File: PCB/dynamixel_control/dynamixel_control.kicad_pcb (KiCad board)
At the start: 4 copper layers, 36 x 56 mm, 57 parts, among them J1 12V, J11 Dynamixel TTL, J12 Dynamixel TTL, J2 RS232, J3 5V, J4 3.3V, J5 I2C, J6 Debug Uart, J8 Dynamixel TTL, Q1 SSM3J372R, Q2 IPD068P03L3GATMA1, Q3 T2N7002AK, SW1 LIMIT_SWITCH, U1 R-78E5.0-0.5, U2 SN74AHC1G14, U3 LM810M3-4.63, U4 Teensy_4.0, U5 MAX3221E, U6 ICM-40627, U7 SN74LV1T34, U8 SN74LVC2G241

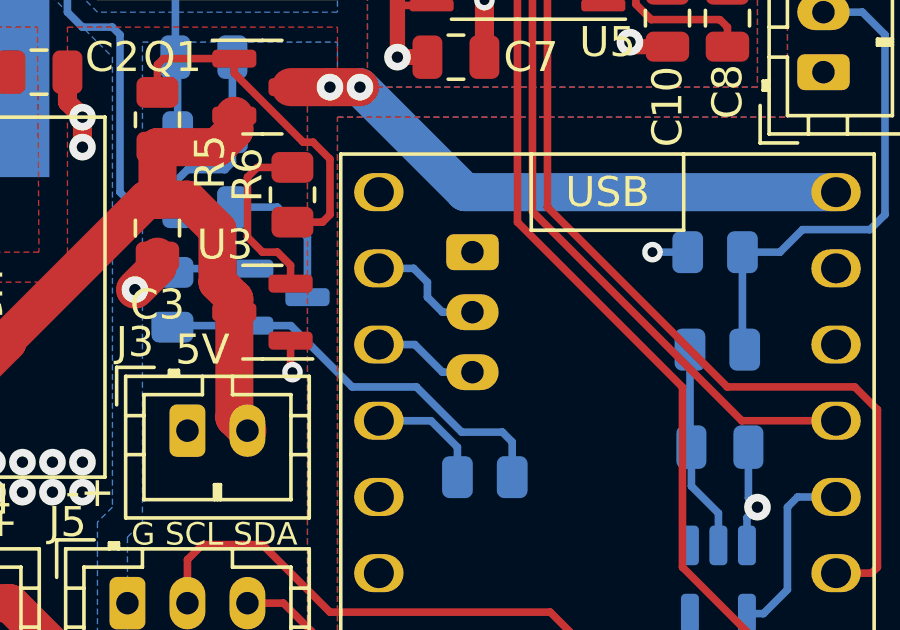
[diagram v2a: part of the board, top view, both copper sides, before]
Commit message: Change MAX3221E by SN65C3221E.
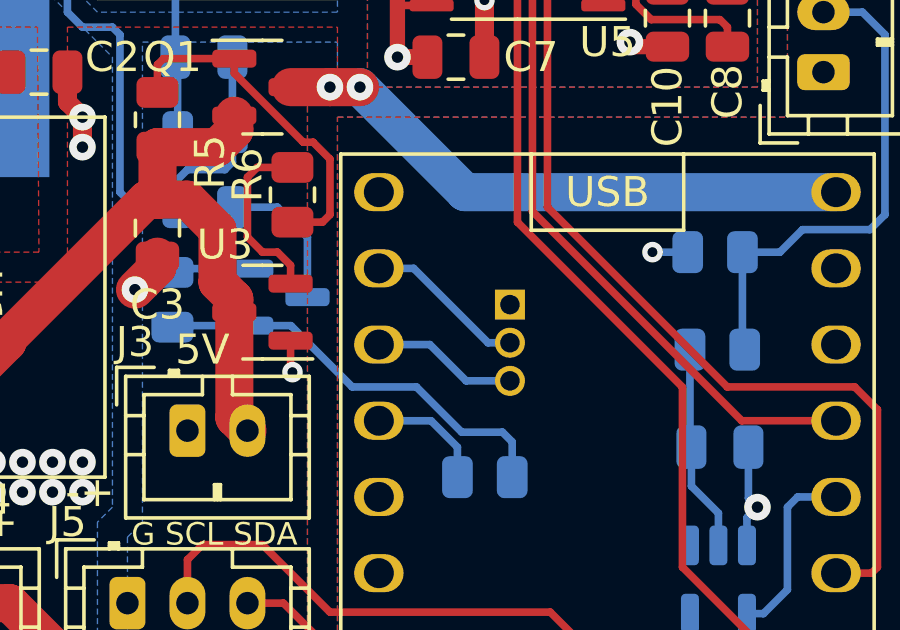
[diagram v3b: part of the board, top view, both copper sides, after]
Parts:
- J6: footprint Connector_JST:JST_PH_B3B-PH-K_1x03_P2.00mm_Vertical -> Connector_PinHeader_1.27mm:PinHeader_1x03_P1.27mm_Vertical
- U5: value MAX3221E -> SN65C3221E
- moved J6 2.15 mm to (42.2, 44.2), turned to 180 degrees
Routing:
- net /DEBUG_UART_RX: track 4.02 -> 5.40 mm
- net /DEBUG_UART_TX: track 3.50 -> 4.87 mm
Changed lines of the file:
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@@
       (effects (font (size 1 1) (thickness 0.15)))
     )
-    (fp_text value "MAX3221E" (at 0 3.45) (layer "F.Fab")
+    (fp_text value "SN65C3221E" (at 0 3.45) (layer "F.Fab")
       (effects (font (size 1 1) (thickness 0.15)))
     )
@@
     )
   )
-  (footprint "Connector_JST:JST_PH_B3B-PH-K_1x03_P2.00mm_Vertical" (layer "B.Cu")
-    (at 41 42.5 -90)
-    (descr "JST PH series connector, B3B-PH-K (http://www.jst-mfg.com/product/pdf/eng/ePH.pdf), generated with kicad-footprint-generator")
-    (tags "connector JST PH side entry")
-    (property "Sheetfile" "dynamixel_control.kicad_sch")
-    (property "Sheetname" "")
-    (attr through_hole)
-    (fp_text reference "J6" (at -1.5 -4 180) (layer "B.SilkS")
-      (effects (font (size 1 1) (thickness 0.15)) (justify mirror))
-    )
-    (fp_text value "Debug Uart" (at 2 -4 90) (layer "B.Fab")
-      (effects (font (size 1 1) (thickness 0.15)) (justify mirror))
-    )
-    (fp_text user "${REFERENCE}" (at 2 -1.5 90) (layer "B.Fab")
-      (effects (font (size 1 1) (thickness 0.15)) (justify mirror))
-    )
-    (fp_line (start 5.45 -2.3) (end 5.45 1.2) (layer "B.SilkS") (width 0.12))
-    (fp_line (start -2.36 2.11) (end -2.36 0.86) (layer "B.SilkS") (width 0.12))
-    (fp_line (start -2.06 -0.8) (end -1.45 -0.8) (layer "B.SilkS") (width 0.12))
-    (fp_line (start 0.9 -1.8) (end 1.1 -1.8) (layer "B.SilkS") (width 0.12))
-    (fp_line (start -1.11 2.11) (end -2.36 2.11) (layer "B.SilkS") (width 0.12))
-    (fp_line (start 0.5 1.81) (end 0.5 1.2) (layer "B.SilkS") (width 0.12))
-    (fp_line (start -2.06 -2.91) (end 6.06 -2.91) (layer "B.SilkS") (width 0.12))
-    (fp_line (start 1.1 -1.8) (end 1.1 -2.3) (layer "B.SilkS") (width 0.12))
-    (fp_line (start -0.3 1.91) (end -0.6 1.91) (layer "B.SilkS") (width 0.12))
-    (fp_line (start 5.45 1.2) (end 3.5 1.2) (layer "B.SilkS") (width 0.12))
-    (fp_line (start 3.5 1.2) (end 3.5 1.81) (layer "B.SilkS") (width 0.12))
-    (fp_line (start 0.9 -2.3) (end 0.9 -1.8) (layer "B.SilkS") (width 0.12))
-    (fp_line (start -1.45 -2.3) (end 5.45 -2.3) (layer "B.SilkS") (width 0.12))
-    (fp_line (start 6.06 1.81) (end -2.06 1.81) (layer "B.SilkS") (width 0.12))
-    (fp_line (start 6.06 -2.91) (end 6.06 1.81) (layer "B.SilkS") (width 0.12))
-    (fp_line (start 2.9 -2.3) (end 2.9 -1.8) (layer "B.SilkS") (width 0.12))
-    (fp_line (start 2.9 -1.8) (end 3.1 -1.8) (layer "B.SilkS") (width 0.12))
-    (fp_line (start 3 -2.3) (end 3 -1.8) (layer "B.SilkS") (width 0.12))
-    (fp_line (start -1.45 1.2) (end -1.45 -2.3) (layer "B.SilkS") (width 0.12))
-    (fp_line (start 0.5 1.2) (end -1.45 1.2) (layer "B.SilkS") (width 0.12))
-    (fp_line (start -0.6 2.01) (end -0.6 1.81) (layer "B.SilkS") (width 0.12))
-    (fp_line (start -0.3 2.01) (end -0.6 2.01) (layer "B.SilkS") (width 0.12))
-    (fp_line (start 6.06 -0.8) (end 5.45 -0.8) (layer "B.SilkS") (width 0.12))
-    (fp_line (start 6.06 0.5) (end 5.45 0.5) (layer "B.SilkS") (width 0.12))
-    (fp_line (start -2.06 0.5) (end -1.45 0.5) (layer "B.SilkS") (width 0.12))
-    (fp_line (start 1 -2.3) (end 1 -1.8) (layer "B.SilkS") (width 0.12))
-    (fp_line (start 3.1 -1.8) (end 3.1 -2.3) (layer "B.SilkS") (width 0.12))
-    (fp_line (start -2.06 1.81) (end -2.06 -2.91) (layer "B.SilkS") (width 0.12))
-    (fp_line (start -0.3 1.81) (end -0.3 2.01) (layer "B.SilkS") (width 0.12))
-    (fp_line (start -2.45 -3.3) (end 6.45 -3.3) (layer "B.CrtYd") (width 0.05))
-    (fp_line (start 6.45 2.2) (end -2.45 2.2) (layer "B.CrtYd") (width 0.05))
-    (fp_line (start -2.45 2.2) (end -2.45 -3.3) (layer "B.CrtYd") (width 0.05))
-    (fp_line (start 6.45 -3.3) (end 6.45 2.2) (layer "B.CrtYd") (width 0.05))
-    (fp_line (start -1.95 1.7) (end -1.95 -2.8) (layer "B.Fab") (width 0.1))
-    (fp_line (start -1.11 2.11) (end -2.36 2.11) (layer "B.Fab") (width 0.1))
-    (fp_line (start 5.95 1.7) (end -1.95 1.7) (layer "B.Fab") (width 0.1))
-    (fp_line (start -2.36 2.11) (end -2.36 0.86) (layer "B.Fab") (width 0.1))
-    (fp_line (start 5.95 -2.8) (end 5.95 1.7) (layer "B.Fab") (width 0.1))
-    (fp_line (start -1.95 -2.8) (end 5.95 -2.8) (layer "B.Fab") (width 0.1))
-    (pad "1" thru_hole roundrect (at 0 0 270) (size 1.2 1.75) (drill 0.75) (layers *.Cu *.Mask) (roundrect_rratio 0.208333)
-      (net 2 "GND") (pinfunction "Pin_1") (pintype "passive"))
-    (pad "2" thru_hole oval (at 2 0 270) (size 1.2 1.75) (drill 0.75) (layers *.Cu *.Mask)
-      (net 50 "/DEBUG_UART_RX") (pinfunction "Pin_2") (pintype "passive"))
-    (pad "3" thru_hole oval (at 4 0 270) (size 1.2 1.75) (drill 0.75) (layers *.Cu *.Mask)
-      (net 51 "/DEBUG_UART_TX") (pinfunction "Pin_3") (pintype "passive"))
-    (model "${KICAD6_3DMODEL_DIR}/Connector_JST.3dshapes/JST_PH_B3B-PH-K_1x03_P2.00mm_Vertical.wrl"
-      (offset (xyz 0 0 0))
-      (scale (xyz 1 1 1))
-      (rotate (xyz 0 0 0))
-    )
-  )
   (footprint "Resistor_SMD:R_0805_2012Metric" (layer "B.Cu")
     (at 49.0875 42.5)
@@
       (net 6 "Net-(C5-Pad1)") (pintype "passive"))
     (model "${KICAD6_3DMODEL_DIR}/Resistor_SMD.3dshapes/R_0805_2012Metric.wrl"
+      (offset (xyz 0 0 0))
+      (scale (xyz 1 1 1))
+      (rotate (xyz 0 0 0))
+    )
+  )
+  (footprint "Connector_PinHeader_1.27mm:PinHeader_1x03_P1.27mm_Vertical" (layer "B.Cu")
+    (at 42.25 44.25 180)
+    (descr "Through hole straight pin header, 1x03, 1.27mm pitch, single row")
+    (tags "Through hole pin header THT 1x03 1.27mm single row")
+    (property "Sheetfile" "dynamixel_control.kicad_sch")
+    (property "Sheetname" "")
+    (attr through_hole)
+    (fp_text reference "J6" (at 0 1.695) (layer "B.SilkS")
+      (effects (font (size 1 1) (thickness 0.15)) (justify mirror))
+    )
+    (fp_text value "Debug Uart" (at 0 -4.235) (layer "B.Fab")
+      (effects (font (size 1 1) (thickness 0.15)) (justify mirror))
+    )
+    (fp_text user "${REFERENCE}" (at 0 -1.27 90) (layer "B.Fab")
+      (effects (font (size 1 1) (thickness 0.15)) (justify mirror))
+    )
+    (fp_line (start -1.11 -0.76) (end -1.11 -3.235) (layer "B.SilkS") (width 0.12))
+    (fp_line (start 0.563471 -0.76) (end 1.11 -0.76) (layer "B.SilkS") (width 0.12))
+    (fp_line (start 1.11 -0.76) (end 1.11 -3.235) (layer "B.SilkS") (width 0.12))
+    (fp_line (start -1.11 0) (end -1.11 0.76) (layer "B.SilkS") (width 0.12))
+    (fp_line (start -1.11 0.76) (end 0 0.76) (layer "B.SilkS") (width 0.12))
+    (fp_line (start -1.11 -0.76) (end -0.563471 -0.76) (layer "B.SilkS") (width 0.12))
+    (fp_line (start 0.30753 -3.235) (end 1.11 -3.235) (layer "B.SilkS") (width 0.12))
+    (fp_line (start -1.11 -3.235) (end -0.30753 -3.235) (layer "B.SilkS") (width 0.12))
+    (fp_line (start -1.55 -3.7) (end 1.55 -3.7) (layer "B.CrtYd") (width 0.05))
+    (fp_line (start -1.55 1.15) (end -1.55 -3.7) (layer "B.CrtYd") (width 0.05))
+    (fp_line (start 1.55 1.15) (end -1.55 1.15) (layer "B.CrtYd") (width 0.05))
+    (fp_line (start 1.55 -3.7) (end 1.55 1.15) (layer "B.CrtYd") (width 0.05))
+    (fp_line (start -0.525 0.635) (end 1.05 0.635) (layer "B.Fab") (width 0.1))
+    (fp_line (start -1.05 -3.175) (end -1.05 0.11) (layer "B.Fab") (width 0.1))
+    (fp_line (start 1.05 0.635) (end 1.05 -3.175) (layer "B.Fab") (width 0.1))
+    (fp_line (start 1.05 -3.175) (end -1.05 -3.175) (layer "B.Fab") (width 0.1))
+    (fp_line (start -1.05 0.11) (end -0.525 0.635) (layer "B.Fab") (width 0.1))
+    (pad "1" thru_hole rect (at 0 0 180) (size 1 1) (drill 0.65) (layers *.Cu *.Mask)
+      (net 2 "GND") (pinfunction "Pin_1") (pintype "passive"))
+    (pad "2" thru_hole oval (at 0 -1.27 180) (size 1 1) (drill 0.65) (layers *.Cu *.Mask)
+      (net 50 "/DEBUG_UART_RX") (pinfunction "Pin_2") (pintype "passive"))
+    (pad "3" thru_hole oval (at 0 -2.54 180) (size 1 1) (drill 0.65) (layers *.Cu *.Mask)
+      (net 51 "/DEBUG_UART_TX") (pinfunction "Pin_3") (pintype "passive"))
+    (model "${KICAD6_3DMODEL_DIR}/Connector_PinHeader_1.27mm.3dshapes/PinHeader_1x03_P1.27mm_Vertical.wrl"
       (offset (xyz 0 0 0))
       (scale (xyz 1 1 1))
@@
   (segment (start 34 69.5) (end 33.75 69.25) (width 0.254) (layer "B.Cu") (net 49))
   (segment (start 33.75 69.25) (end 33.75 62) (width 0.254) (layer "B.Cu") (net 49))
-  (segment (start 37.88 43.04) (end 39.04 43.04) (width 0.254) (layer "B.Cu") (net 50))
-  (segment (start 39.04 43.04) (end 39.5 43.5) (width 0.254) (layer "B.Cu") (net 50))
-  (segment (start 41 44.5) (end 40 44.5) (width 0.254) (layer "B.Cu") (net 50))
-  (segment (start 40 44.5) (end 39.5 44) (width 0.254) (layer "B.Cu") (net 50))
-  (segment (start 39.5 43.5) (end 39.5 44) (width 0.254) (layer "B.Cu") (net 50))
-  (segment (start 39.08 45.58) (end 37.88 45.58) (width 0.254) (layer "B.Cu") (net 51))
-  (segment (start 41 46.5) (end 40 46.5) (width 0.254) (layer "B.Cu") (net 51))
-  (segment (start 40 46.5) (end 39.08 45.58) (width 0.254) (layer "B.Cu") (net 51))
+  (segment (start 39.04 43.04) (end 37.88 43.04) (width 0.254) (layer "B.Cu") (net 50))
+  (segment (start 41.52 45.52) (end 42.25 45.52) (width 0.254) (layer "B.Cu") (net 50))
+  (segment (start 39.04 43.04) (end 41.52 45.52) (width 0.254) (layer "B.Cu") (net 50))
+  (segment (start 39.58 45.58) (end 37.88 45.58) (width 0.254) (layer "B.Cu") (net 51))
+  (segment (start 39.58 45.58) (end 40.79 46.79) (width 0.254) (layer "B.Cu") (net 51))
+  (segment (start 42.25 46.79) (end 40.79 46.79) (width 0.254) (layer "B.Cu") (net 51))
   (zone (net 2) (net_name "GND") (layer "F.Cu") (hatch edge 0.508)
     (connect_pads yes (clearance 0.508))

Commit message: Fix PCBs.
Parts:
- removed J3: 5V, Connector_JST:JST_PH_B2B-PH-K_1x02_P2.00mm_Vertical
- removed J4: 3.3V, Connector_JST:JST_PH_B2B-PH-K_1x02_P2.00mm_Vertical
- removed J5: I2C, Connector_JST:JST_PH_B3B-PH-K_1x03_P2.00mm_Vertical
- added C14: 10µF/25V, Capacitor_SMD:C_0805_2012Metric, F.Cu at (26.4, 51.5)
- added L2: 12µH (RLS-126), Inductor_SMD:L_1812_4532Metric, F.Cu at (25.4, 55.0)
- added R2: 10k, Resistor_SMD:R_0805_2012Metric, F.Cu at (33.4, 56.5)
- moved C3 12.7 mm to (22.5, 51.5), turned to 0 degrees
- moved C12 0.50 mm to (50.0, 67.0)
- moved C13 0.50 mm to (50.0, 70.5)
- moved R18 0.50 mm to (31.0, 44.6)
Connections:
- C3 pad 1: +5V -> Net-(C3-Pad1)
- U1 pad 3: +5V -> Net-(C3-Pad1)
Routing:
- net /I2C_SCL: track 44.7 -> 20.4 mm
- net +3.3V: track 53.1 -> 34.3 mm, vias 11 -> 12
- net /I2C_SDA: track 31.5 -> 17.2 mm
- net Net-(C3-Pad1): track 0.00 -> 9.49 mm
- net Net-(R2-Pad2): track 10.2 -> 19.5 mm
- net Net-(C2-Pad1): track 0.00 -> 9.19 mm
- net +5V: track 61.9 -> 53.6 mm, vias 1 -> 2
- net GND: track 52.1 -> 50.0 mm
- net /Dynamixel/DYNAMIXEL_POWER: vias 16 -> 0
- added copper zone on In2.Cu, net GND
- removed copper zone on In2.Cu, net /Dynamixel/DYNAMIXEL_POWER
- removed copper zone on F.Cu, net Net-(C2-Pad1)
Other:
- board text removed: "-+"
- board text removed: "3.3V -+"
- board text removed: "5V"
- board text removed: "G SCL SDA"

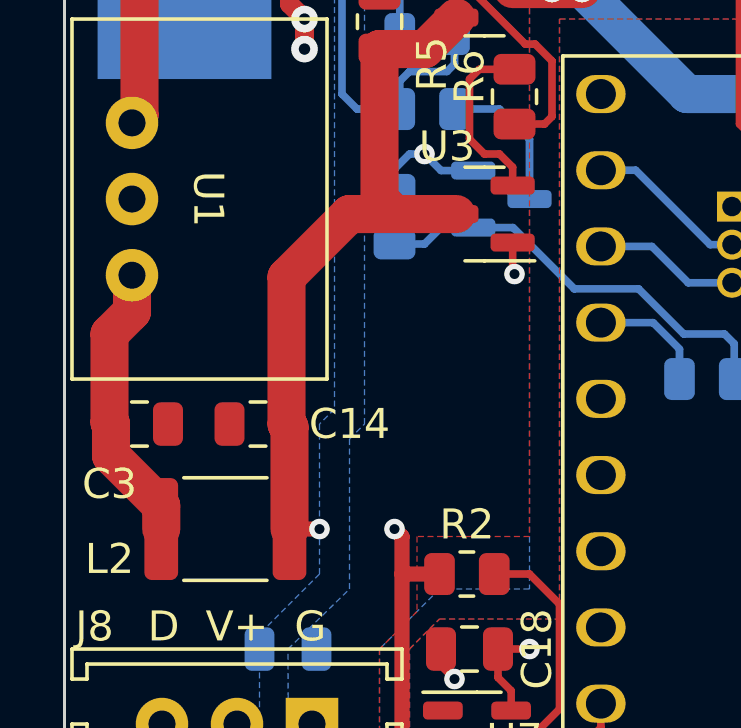
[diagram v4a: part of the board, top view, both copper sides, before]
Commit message: Add a PI filter to buck_boost. Fix ringing for other PI filters.
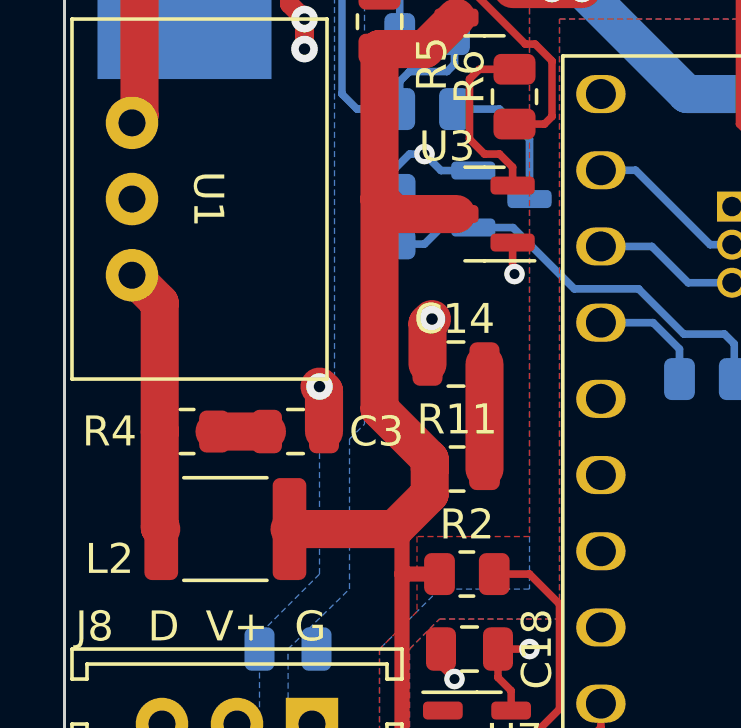
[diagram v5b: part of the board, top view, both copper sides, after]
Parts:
- added R11: 0, Resistor_SMD:R_0805_2012Metric, F.Cu at (33.1, 53.0)
- added R4: 0, Resistor_SMD:R_0805_2012Metric, F.Cu at (24.1, 51.8)
- moved C14 6.90 mm to (33.0, 49.5)
- moved C3 5.21 mm to (27.7, 51.8)
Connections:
- C14 pad 1: +5V -> Net-(C14-Pad1)
- L2 pad 1: Net-(C3-Pad1) -> Net-(L2-Pad1)
- U1 pad 3: Net-(C3-Pad1) -> Net-(L2-Pad1)
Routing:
- net Net-(L2-Pad1): track 0.00 -> 8.86 mm
- net Net-(C3-Pad1): track 9.49 -> 1.75 mm
- net Net-(C14-Pad1): track 0.00 -> 3.50 mm
- net GND: track 50.0 -> 53.1 mm, vias 36 -> 38
- net +5V: track 53.6 -> 52.5 mm, vias 2 -> 0

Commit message: Update PCBs
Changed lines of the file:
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@@
+      (effects (font (size 1 1) (thickness 0.15)))
+    )
+    (fp_text user "y" (at 1 4 unlocked) (layer "F.SilkS")
       (effects (font (size 1 1) (thickness 0.15)))
     )
@@
       (effects (font (size 1 1) (thickness 0.15)))
     )
-    (fp_text user "y" (at 1 4 unlocked) (layer "F.SilkS")
-      (effects (font (size 1 1) (thickness 0.15)))
-    )
     (fp_text user "${REFERENCE}" (at 0 8 unlocked) (layer "F.Fab")
       (effects (font (size 1 1) (thickness 0.15)))
     )
+    (fp_line (start 1.5 1.25) (end -1.5 1.25) (layer "F.SilkS") (width 0.12))
+    (fp_line (start 1.5 5) (end 1.25 5.25) (layer "F.SilkS") (width 0.12))
+    (fp_line (start -1.5 -1.25) (end 1.5 -1.25) (layer "F.SilkS") (width 0.12))
     (fp_line (start -1.5 1.25) (end -1.5 -1.25) (layer "F.SilkS") (width 0.12))
+    (fp_line (start 1.5 3) (end 1 3.5) (layer "F.SilkS") (width 0.12))
     (fp_line (start 3.5 5) (end 3 4.5) (layer "F.SilkS") (width 0.12))
-    (fp_line (start 1.5 1.25) (end -1.5 1.25) (layer "F.SilkS") (width 0.12))
+    (fp_line (start 1.5 3) (end 2 3.5) (layer "F.SilkS") (width 0.12))
+    (fp_line (start 1.5 5) (end 1.5 3) (layer "F.SilkS") (width 0.12))
+    (fp_line (start 3.5 5) (end 3 5.5) (layer "F.SilkS") (width 0.12))
+    (fp_line (start 1.5 5) (end 3.5 5) (layer "F.SilkS") (width 0.12))
     (fp_line (start 1.5 -1.25) (end 1.5 1.25) (layer "F.SilkS") (width 0.12))
-    (fp_line (start -1.5 -1.25) (end 1.5 -1.25) (layer "F.SilkS") (width 0.12))
-    (fp_line (start 1.5 5) (end 3.5 5) (layer "F.SilkS") (width 0.12))
-    (fp_line (start 1.5 3) (end 2 3.5) (layer "F.SilkS") (width 0.12))
-    (fp_line (start 1.5 5) (end 1.25 5.25) (layer "F.SilkS") (width 0.12))
-    (fp_line (start 1.5 5) (end 1.5 3) (layer "F.SilkS") (width 0.12))
-    (fp_line (start 1.5 3) (end 1 3.5) (layer "F.SilkS") (width 0.12))
-    (fp_line (start 3.5 5) (end 3 5.5) (layer "F.SilkS") (width 0.12))
+    (fp_circle (center -2 -1.75) (end -1.75 -1.75) (layer "F.SilkS") (width 0.12) (fill solid))
     (fp_circle (center 1.5 5) (end 1.853553 5) (layer "F.SilkS") (width 0.12) (fill solid))
+    (fp_line (start -2.5 -2.25) (end 2.5 -2.25) (layer "F.CrtYd") (width 0.05))
     (fp_line (start 2.5 -2.25) (end 2.5 2.25) (layer "F.CrtYd") (width 0.05))
     (fp_line (start 2.5 2.25) (end -2.5 2.25) (layer "F.CrtYd") (width 0.05))
     (fp_line (start -2.5 2.25) (end -2.5 -2.25) (layer "F.CrtYd") (width 0.05))
-    (fp_line (start -2.5 -2.25) (end 2.5 -2.25) (layer "F.CrtYd") (width 0.05))
     (pad "1" smd rect (at -1.1625 -0.75) (size 1 0.3) (drill (offset -0.2625 0)) (layers "F.Cu" "F.Paste" "F.Mask")
       (net 27 "Net-(R10-Pad1)") (pinfunction "AP_SDO/AP_AD0") (pintype "bidirectional") (solder_mask_margin 0.05))
@@
     (pad "5" smd rect (at -0.5 0.9125) (size 0.3 1) (drill (offset 0 0.2625)) (layers "F.Cu" "F.Paste" "F.Mask")
       (net 5 "+3.3V") (pinfunction "VDDIO") (pintype "power_in") (solder_mask_margin 0.05))
-    (pad "6" smd rect (at 0.5 0.9125) (size 0.3 1) (drill (offset 0 0.2625)) (layers "F.Cu" "F.Paste" "F.Mask")
+    (pad "6" smd rect (at -1.1625 0.25) (size 1 0.3) (drill (offset -0.2625 0)) (layers "F.Cu" "F.Paste" "F.Mask")
+      (net 2 "GND") (pinfunction "GND") (pintype "power_in") (solder_mask_margin 0.05))
+    (pad "6" smd rect (at 0 0.9125) (size 0.3 1) (drill (offset 0 0.2625)) (layers "F.Cu" "F.Paste" "F.Mask")
       (net 2 "GND") (pinfunction "GND") (pintype "power_in") (solder_mask_margin 0.05))
     (pad "6" smd rect (at 1.1625 -0.25) (size 1 0.3) (drill (offset 0.2625 0)) (layers "F.Cu" "F.Paste" "F.Mask")
       (net 2 "GND") (pinfunction "GND") (pintype "power_in") (solder_mask_margin 0.05))
-    (pad "6" smd rect (at 0 0.9125) (size 0.3 1) (drill (offset 0 0.2625)) (layers "F.Cu" "F.Paste" "F.Mask")
+    (pad "6" smd rect (at 0.5 0.9125) (size 0.3 1) (drill (offset 0 0.2625)) (layers "F.Cu" "F.Paste" "F.Mask")
+      (net 2 "GND") (pinfunction "GND") (pintype "power_in") (solder_mask_margin 0.05))
+    (pad "6" smd rect (at 1.1625 -0.75) (size 1 0.3) (drill (offset 0.2625 0)) (layers "F.Cu" "F.Paste" "F.Mask")
       (net 2 "GND") (pinfunction "GND") (pintype "power_in") (solder_mask_margin 0.05))
     (pad "6" smd rect (at -1.1625 -0.25) (size 1 0.3) (drill (offset -0.2625 0)) (layers "F.Cu" "F.Paste" "F.Mask")
       (net 2 "GND") (pinfunction "GND") (pintype "power_in") (solder_mask_margin 0.05))
-    (pad "6" smd rect (at 1.1625 -0.75) (size 1 0.3) (drill (offset 0.2625 0)) (layers "F.Cu" "F.Paste" "F.Mask")
-      (net 2 "GND") (pinfunction "GND") (pintype "power_in") (solder_mask_margin 0.05))
-    (pad "6" smd rect (at -1.1625 0.25) (size 1 0.3) (drill (offset -0.2625 0)) (layers "F.Cu" "F.Paste" "F.Mask")
-      (net 2 "GND") (pinfunction "GND") (pintype "power_in") (solder_mask_margin 0.05))
     (pad "8" smd rect (at 1.1625 0.75) (size 1 0.3) (drill (offset 0.2625 0)) (layers "F.Cu" "F.Paste" "F.Mask")
